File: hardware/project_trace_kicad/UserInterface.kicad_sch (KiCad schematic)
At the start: 13 parts, among them J4 Conn_01x07_Pin, J5 Conn_01x07_Socket, SW1 SW_Push, SW2 SW_Push, SW3 RotaryEncoder, SW4 RotaryEncoder, U1 SBC-OLED01.3

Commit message: Fix hardware-digital merge
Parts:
- SW1, SW2, SW3, SW4, U1: DigikeyPN (none) -> N/A
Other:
- moved on the sheet: R1, R2, R3, R4, SW4

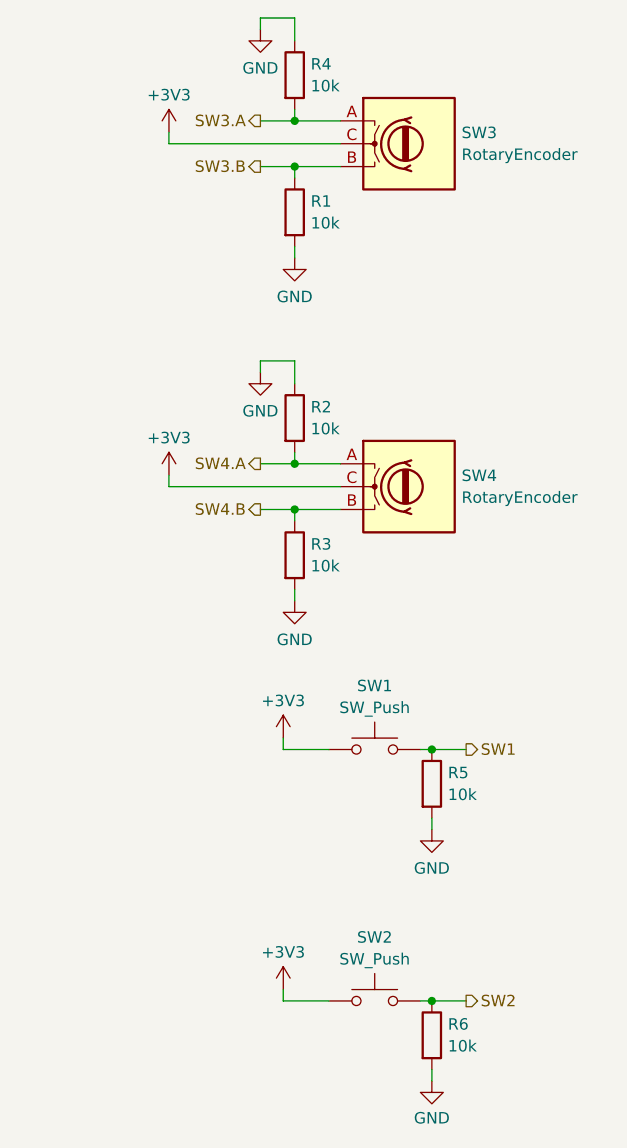
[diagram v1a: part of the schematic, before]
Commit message: power added to nucleo and GPIO for ranging/ac/dc added to Nucleo
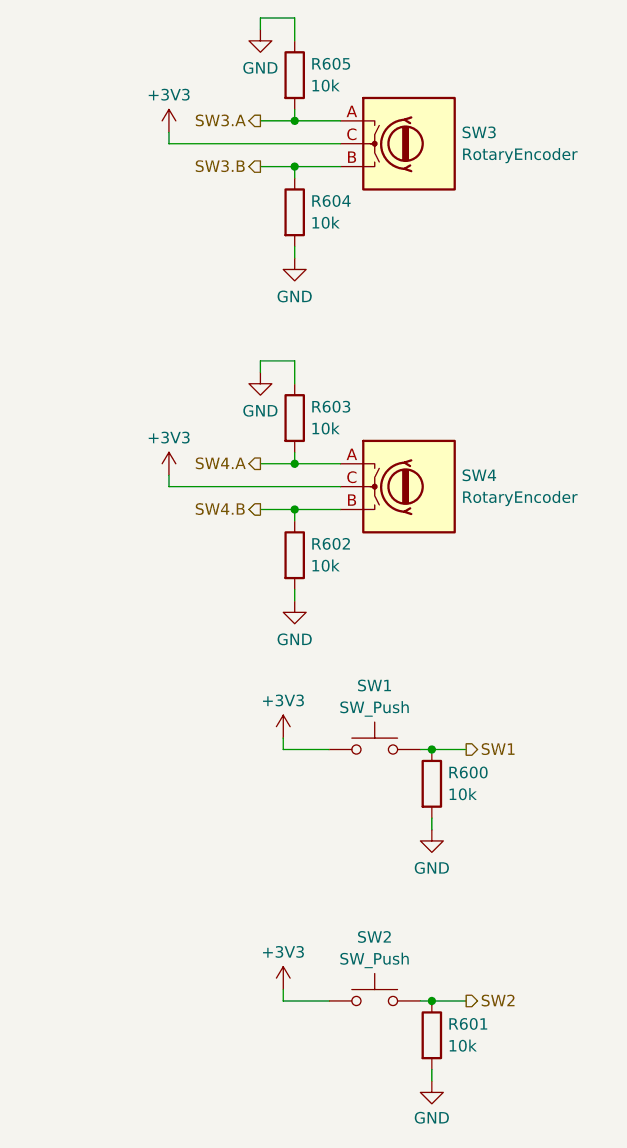
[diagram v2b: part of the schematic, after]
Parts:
- removed R1, R2, R3, R4, R6: 10k, symbol Device:R
- added R601, R602, R603, R604, R605: 10k, Resistor_THT:R_Axial_DIN0207_L6.3mm_D2.5mm_P10.16mm_Horizontal, symbol Device:R
- R600: renamed from R5; footprint (none) -> Resistor_THT:R_Axial_DIN0207_L6.3mm_D2.5mm_P10.16mm_Horizontal
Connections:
- net GND: now also R601.2, R602.2, R603.1, R604.2, R605.1
- net SW2: now also R601.1
- net SW3.A: now also R605.2
- net SW3.B: now also R604.1
- net SW4.A: now also R603.2
- net SW4.B: now also R602.1
